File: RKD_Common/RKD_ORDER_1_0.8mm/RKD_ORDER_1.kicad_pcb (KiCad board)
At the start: 2 copper layers, 98.8 x 99.4 mm, 53 parts, among them SW2 KEY_SWITCH

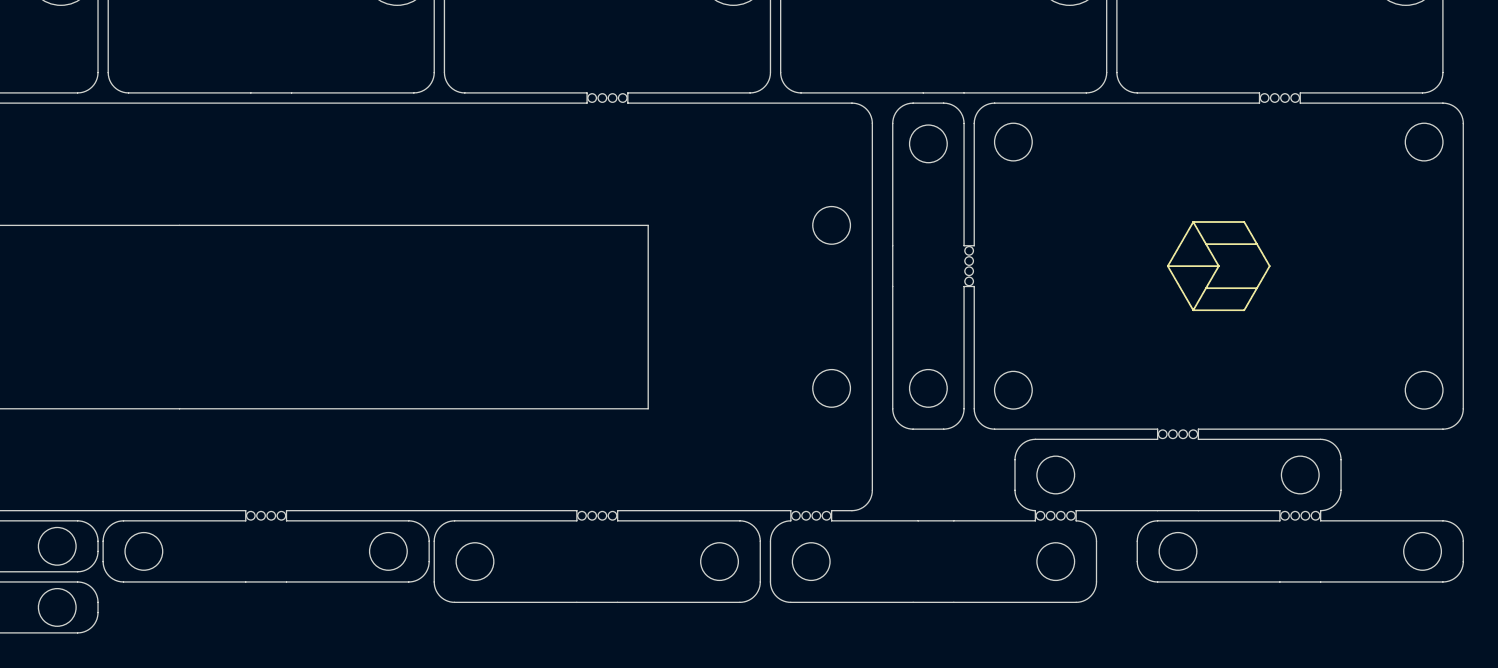
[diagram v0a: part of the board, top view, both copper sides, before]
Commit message: Order用の内容を削減
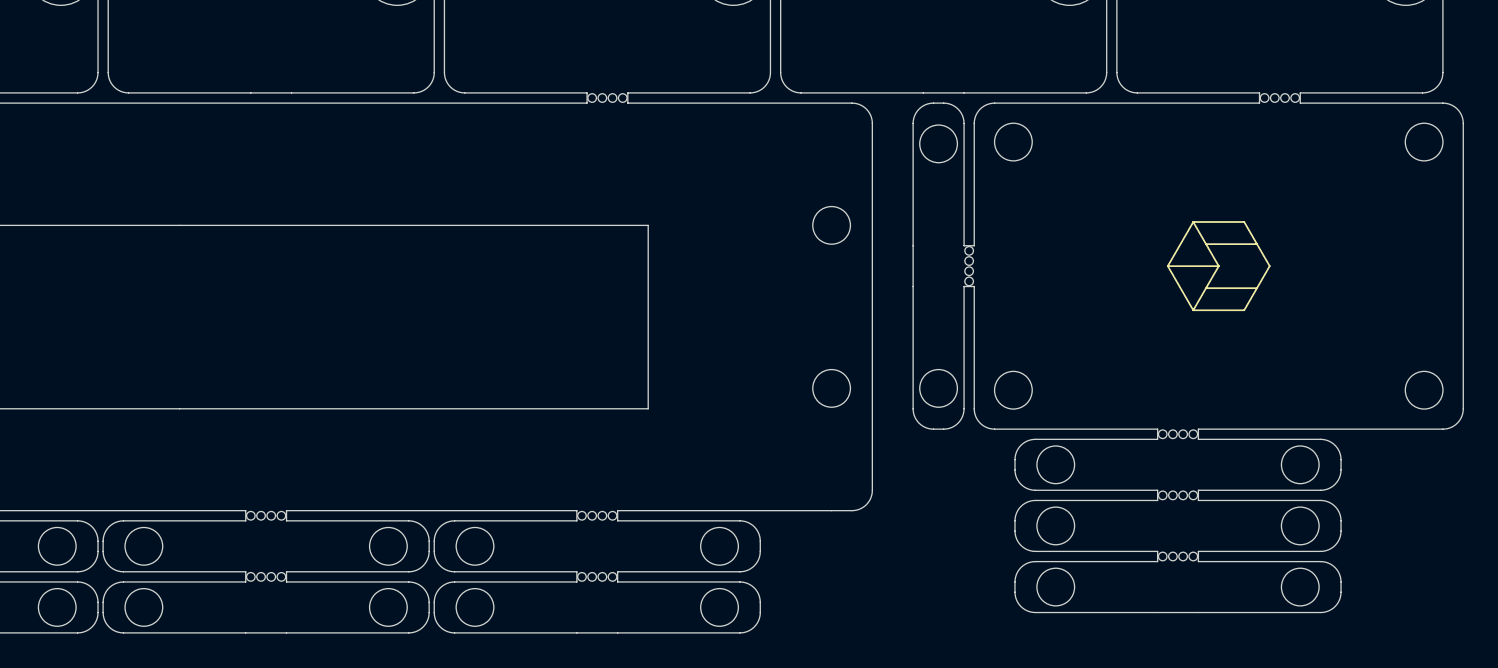
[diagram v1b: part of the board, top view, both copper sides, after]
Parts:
- removed the REF** at (91.7, 149.7)
- removed the REF** at (120.3, 149.7)
- removed the REF** at (106.0, 149.7)
- removed the Ref** at (91.7, 152.4)
- removed the Ref** at (98.5, 128.0)
- removed the Ref** at (106.0, 147.3)
- removed the Ref** at (127.4, 151.8)
- removed the Ref** at (72.0, 152.4)
- removed the Ref** at (120.3, 147.3)
- removed the Ref** at (52.7, 151.8)
- removed the Ref** at (113.1, 151.8)
- removed the Ref** at (98.5, 142.3)
- removed the Ref** at (67.0, 151.8)
- removed the Ref** at (86.3, 152.4)
- removed the Ref** at (106.0, 152.4)
- added REF**: rkd_cutdot, Rikkodo_FootPrint:rkd_cutdot, F.Cu at (113.1, 152.1)
- added REF**: rkd_cutdot, Rikkodo_FootPrint:rkd_cutdot, F.Cu at (113.1, 148.5)
- added REF**: rkd_cutdot, Rikkodo_FootPrint:rkd_cutdot, F.Cu at (59.8, 153.3)
- added REF**: rkd_cutdot, Rikkodo_FootPrint:rkd_cutdot, F.Cu at (79.2, 153.3)
- added Ref**: Val**, kbd_Hole:m2_Screw_Hole, F.Cu at (99.1, 142.3)
- added Ref**: Val**, kbd_Hole:m2_Screw_Hole, F.Cu at (106.0, 146.7)
- added Ref**: Val**, kbd_Hole:m2_Screw_Hole, F.Cu at (52.7, 151.5)
- added Ref**: Val**, kbd_Hole:m2_Screw_Hole, F.Cu at (72.0, 155.1)
- added Ref**: Val**, kbd_Hole:m2_Screw_Hole, F.Cu at (67.0, 151.5)
- added Ref**: Val**, kbd_Hole:m2_Screw_Hole, F.Cu at (52.7, 155.1)
- added Ref**: Val**, kbd_Hole:m2_Screw_Hole, F.Cu at (120.3, 153.9)
- added Ref**: Val**, kbd_Hole:m2_Screw_Hole, F.Cu at (120.3, 150.3)
- added Ref**: Val**, kbd_Hole:m2_Screw_Hole, F.Cu at (86.3, 151.5)
- added Ref**: Val**, kbd_Hole:m2_Screw_Hole, F.Cu at (86.3, 155.1)
- added Ref**: Val**, kbd_Hole:m2_Screw_Hole, F.Cu at (67.0, 155.1)
- added Ref**: Val**, kbd_Hole:m2_Screw_Hole, F.Cu at (99.1, 128.0)
- added Ref**: Val**, kbd_Hole:m2_Screw_Hole, F.Cu at (106.0, 150.3)
- added Ref**: Val**, kbd_Hole:m2_Screw_Hole, F.Cu at (72.0, 151.5)
- added Ref**: Val**, kbd_Hole:m2_Screw_Hole, F.Cu at (106.0, 153.9)
- added Ref**: Val**, kbd_Hole:m2_Screw_Hole, F.Cu at (120.3, 146.7)
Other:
- outline, holes or cut-outs redrawn
- board text removed: "RKD_PGD6 v1.0"
- board text removed: "RKD_PGD7 v1.0"
- board text removed: "RKD_PGD8 v1.0"

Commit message: SekiBall追加
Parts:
- added REF** (x2): rkd_SekiBall_ScrewHall, Rikkodo_FootPrint:rkd_SekiBall_ScrewHall, B.Cu at (115.5, 135.1)
- added REF** (x2): rkd_SekiBall_ScrewHall, Rikkodo_FootPrint:rkd_SekiBall_ScrewHall, B.Cu at (119.1, 72.0)

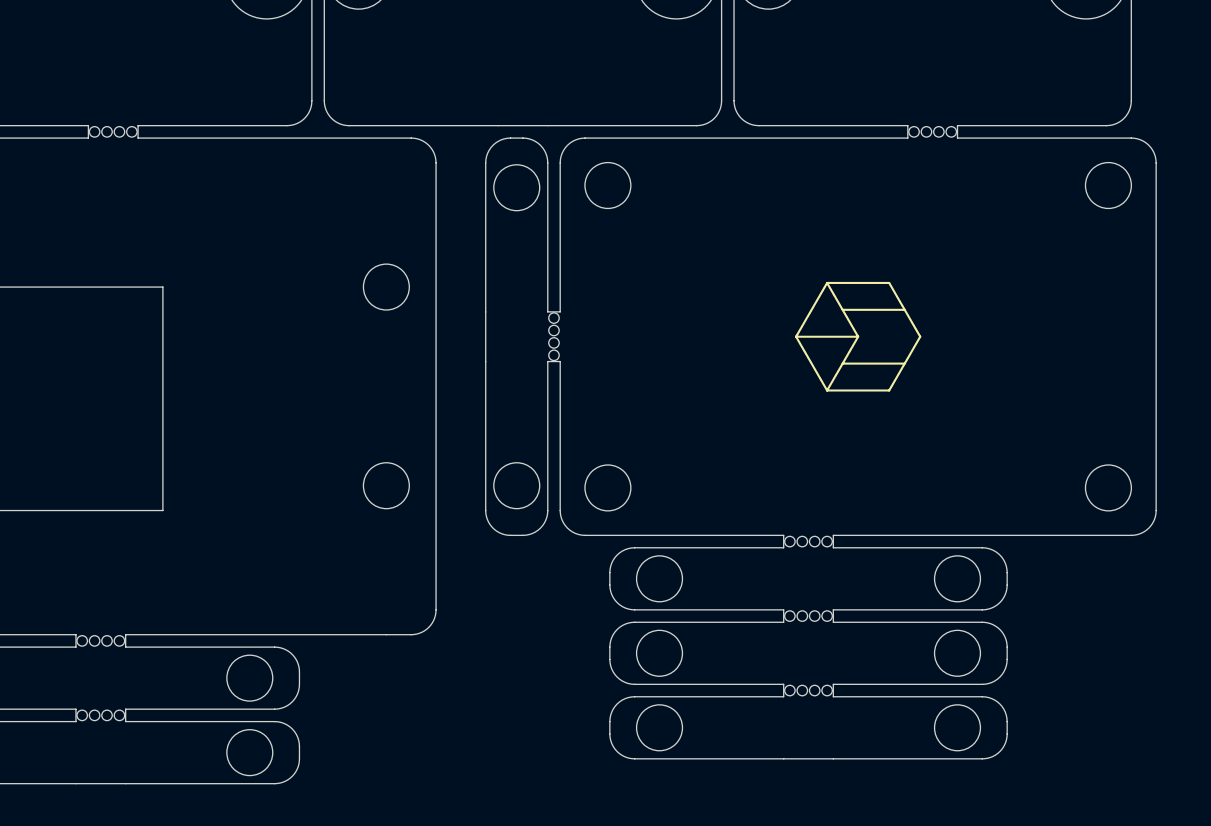
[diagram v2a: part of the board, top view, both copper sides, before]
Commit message: ワッシャー追加
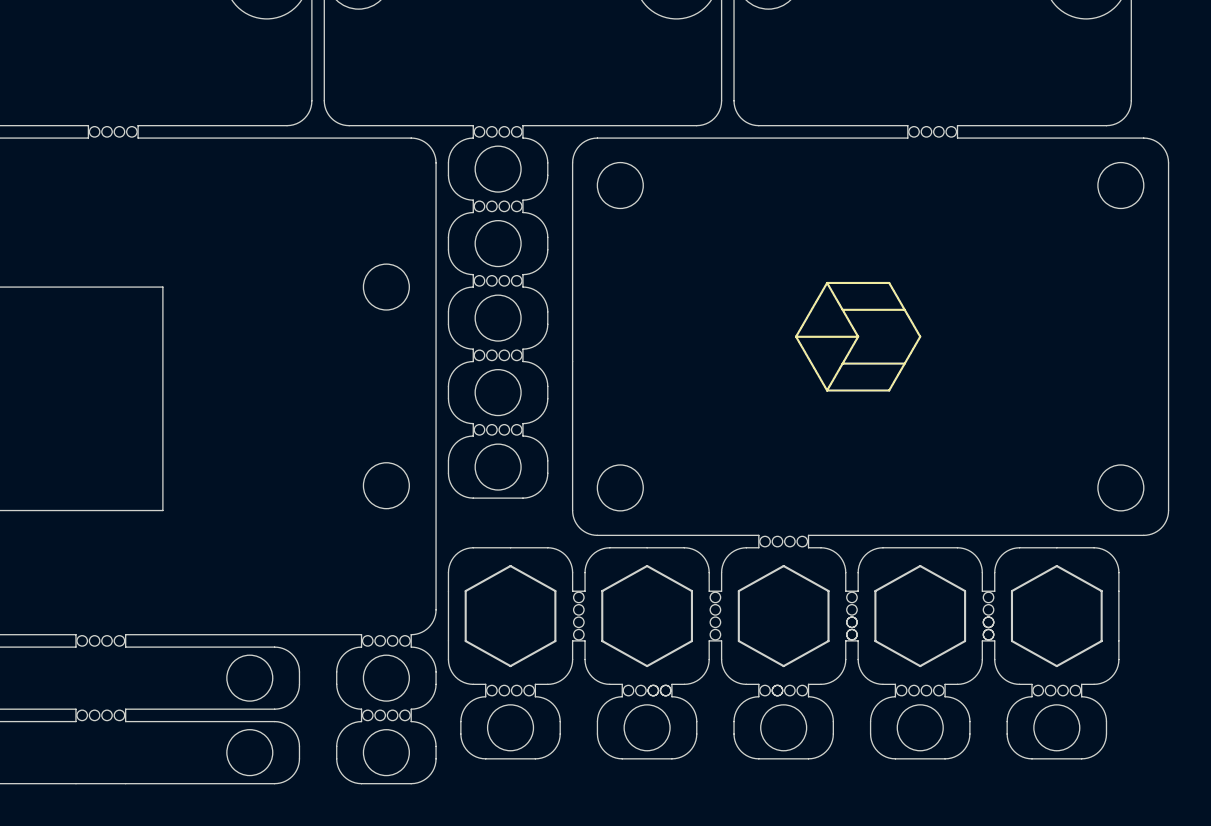
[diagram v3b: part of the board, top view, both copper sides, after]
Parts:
- removed the REF** at (113.1, 152.1)
- removed the REF** at (113.1, 148.5)
- removed the REF** at (100.9, 135.1)
- removed the REF** at (113.1, 145.0)
- removed the Ref** at (99.1, 142.3)
- removed the Ref** at (106.0, 146.7)
- removed the Ref** at (120.3, 153.9)
- removed the Ref** at (120.3, 150.3)
- removed the Ref** at (99.1, 128.0)
- removed the Ref** at (106.0, 150.3)
- removed the Ref** at (106.0, 153.9)
- removed the Ref** at (120.3, 146.7)
- added ?: , , F.Cu at (105.7, 152.1)
- added ?: , , F.Cu at (115.2, 149.4)
- added ?: , , F.Cu at (121.7, 149.4)
- added ?: , , F.Cu at (106.3, 152.1)
- added ?: , , F.Cu at (121.7, 148.8)
- added ?: , , F.Cu at (111.6, 152.1)
- added ?: , , F.Cu at (115.2, 148.8)
- added REF**: rkd_cutdot, Rikkodo_FootPrint:rkd_cutdot, F.Cu at (118.5, 152.1)
- added REF**: rkd_cutdot, Rikkodo_FootPrint:rkd_cutdot, F.Cu at (111.9, 145.0)
- added REF**: rkd_cutdot, Rikkodo_FootPrint:rkd_cutdot, F.Cu at (98.2, 128.9)
- added REF**: rkd_cutdot, Rikkodo_FootPrint:rkd_cutdot, F.Cu at (108.6, 148.5)
- added REF**: rkd_cutdot, Rikkodo_FootPrint:rkd_cutdot, F.Cu at (125.0, 152.1)
- added REF**: rkd_cutdot, Rikkodo_FootPrint:rkd_cutdot, F.Cu at (102.1, 148.5)
- added REF**: rkd_cutdot, Rikkodo_FootPrint:rkd_cutdot, F.Cu at (92.9, 153.3)
- added REF**: rkd_cutdot, Rikkodo_FootPrint:rkd_cutdot, F.Cu at (98.2, 136.0)
- added REF**: rkd_cutdot, Rikkodo_FootPrint:rkd_cutdot, F.Cu at (98.8, 152.1)
- added REF**: rkd_cutdot, Rikkodo_FootPrint:rkd_cutdot, F.Cu at (92.9, 149.7)
- added REF**: rkd_cutdot, Rikkodo_FootPrint:rkd_cutdot, F.Cu at (105.4, 152.1)
- added REF**: rkd_cutdot, Rikkodo_FootPrint:rkd_cutdot, F.Cu at (115.2, 148.5)
- added REF**: rkd_cutdot, Rikkodo_FootPrint:rkd_cutdot, F.Cu at (111.9, 152.1)
- added REF**: rkd_cutdot, Rikkodo_FootPrint:rkd_cutdot, F.Cu at (98.2, 125.3)
- added REF**: rkd_cutdot, Rikkodo_FootPrint:rkd_cutdot, F.Cu at (98.2, 132.5)
- added REF**: rkd_cutdot, Rikkodo_FootPrint:rkd_cutdot, F.Cu at (121.7, 148.5)
- added REF**: rkd_cutdot, Rikkodo_FootPrint:rkd_cutdot, F.Cu at (98.2, 139.6)
- added Ref**: Val**, kbd_Hole:m2_Screw_Hole, F.Cu at (98.2, 127.1)
- added Ref**: Val**, kbd_Hole:m2_Screw_Hole, F.Cu at (105.4, 153.9)
- added Ref**: Val**, kbd_Hole:m2_Screw_Hole, F.Cu at (98.2, 130.7)
- added Ref**: Val**, kbd_Hole:m2_Screw_Hole, F.Cu at (98.2, 134.2)
- added Ref**: Val**, kbd_Hole:m2_Spacer_Hole_hex, F.Cu at (105.4, 148.5)
- added Ref**: Val**, kbd_Hole:m2_Screw_Hole, F.Cu at (92.9, 151.5)
- added Ref**: Val**, kbd_Hole:m2_Screw_Hole, F.Cu at (125.0, 153.9)
- added Ref**: Val**, kbd_Hole:m2_Spacer_Hole_hex, F.Cu at (98.8, 148.5)
- added Ref**: Val**, kbd_Hole:m2_Spacer_Hole_hex, F.Cu at (118.5, 148.5)
- added Ref**: Val**, kbd_Hole:m2_Screw_Hole, F.Cu at (92.9, 155.1)
- added Ref**: Val**, kbd_Hole:m2_Screw_Hole, F.Cu at (118.5, 153.9)
- added Ref**: Val**, kbd_Hole:m2_Spacer_Hole_hex, F.Cu at (111.9, 148.5)
- added Ref**: Val**, kbd_Hole:m2_Spacer_Hole_hex, F.Cu at (125.0, 148.5)
- added Ref**: Val**, kbd_Hole:m2_Screw_Hole, F.Cu at (111.9, 153.9)
- added Ref**: Val**, kbd_Hole:m2_Screw_Hole, F.Cu at (98.8, 153.9)
- added Ref**: Val**, kbd_Hole:m2_Screw_Hole, F.Cu at (98.2, 141.4)
- added Ref**: Val**, kbd_Hole:m2_Screw_Hole, F.Cu at (98.2, 137.8)
- moved Point1 0.60 mm to (116.1, 135.1)
- moved REF** 0.60 mm to (116.1, 135.1) (x2)
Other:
- board size 98.8 x 99.4 mm -> 99.4 x 99.4 mm

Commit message: ORDER 不要パーツ削除
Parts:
- removed the ? at (105.7, 152.1)
- removed the ? at (115.2, 149.4)
- removed the ? at (121.7, 149.4)
- removed the ? at (106.3, 152.1)
- removed the ? at (121.7, 148.8)
- removed the ? at (111.6, 152.1)
- removed the ? at (115.2, 148.8)
- removed the REF** at (118.5, 152.1)
- removed the REF** at (111.9, 145.0)
- removed the REF** at (108.6, 148.5)
- removed the REF** at (125.0, 152.1)
- removed the REF** at (102.1, 148.5)
- removed the REF** at (98.8, 152.1)
- removed the REF** at (105.4, 152.1)
- removed the REF** at (115.2, 148.5)
- removed the REF** at (111.9, 152.1)
- removed the REF** at (121.7, 148.5)
- removed the Ref** at (105.4, 153.9)
- removed the Ref** at (105.4, 148.5)
- removed the Ref** at (125.0, 153.9)
- removed the Ref** at (98.8, 148.5)
- removed the Ref** at (118.5, 148.5)
- removed the Ref** at (118.5, 153.9)
- removed the Ref** at (111.9, 148.5)
- removed the Ref** at (125.0, 148.5)
- removed the Ref** at (111.9, 153.9)
- removed the Ref** at (98.8, 153.9)
- added ?: , , F.Cu at (127.7, 148.5)
- added ?: , , F.Cu at (107.5, 148.5)
- added ?: , , F.Cu at (122.6, 148.5)
- added ?: , , F.Cu at (117.6, 148.5)
- added ?: , , F.Cu at (112.5, 148.5)
- added REF**: rkd_cutdot, Rikkodo_FootPrint:rkd_cutdot, F.Cu at (117.9, 152.1)
- added REF**: rkd_cutdot, Rikkodo_FootPrint:rkd_cutdot, F.Cu at (107.8, 152.1)
- added REF**: rkd_cutdot, Rikkodo_FootPrint:rkd_cutdot, F.Cu at (117.9, 145.0)
- added REF**: rkd_cutdot, Rikkodo_FootPrint:rkd_cutdot, F.Cu at (122.9, 148.5)
- added REF**: rkd_cutdot, Rikkodo_FootPrint:rkd_cutdot, F.Cu at (107.8, 148.5)
- added REF**: rkd_cutdot, Rikkodo_FootPrint:rkd_cutdot, F.Cu at (122.9, 152.1)
- added REF**: rkd_cutdot, Rikkodo_FootPrint:rkd_cutdot, F.Cu at (107.8, 145.0)
- added REF**: rkd_cutdot, Rikkodo_FootPrint:rkd_cutdot, F.Cu at (112.8, 152.1)
- added REF**: rkd_cutdot, Rikkodo_FootPrint:rkd_cutdot, F.Cu at (128.0, 152.1)
- added REF**: rkd_cutdot, Rikkodo_FootPrint:rkd_cutdot, F.Cu at (112.8, 148.5)
- added REF**: rkd_cutdot, Rikkodo_FootPrint:rkd_cutdot, F.Cu at (122.9, 145.0)
- added REF**: rkd_cutdot, Rikkodo_FootPrint:rkd_cutdot, F.Cu at (128.0, 145.0)
- added REF**: rkd_cutdot, Rikkodo_FootPrint:rkd_cutdot, F.Cu at (117.9, 148.5)
- added REF**: rkd_cutdot, Rikkodo_FootPrint:rkd_cutdot, F.Cu at (98.2, 146.7)
- added REF**: rkd_LOGO, Rikkodo_FootPrint:rkd_LOGO, F.Cu at (88.1, 138.1)
- added REF**: rkd_cutdot, Rikkodo_FootPrint:rkd_cutdot, F.Cu at (128.0, 148.5)
- added REF**: rkd_cutdot, Rikkodo_FootPrint:rkd_cutdot, F.Cu at (98.2, 150.3)
- added REF**: rkd_cutdot, Rikkodo_FootPrint:rkd_cutdot, F.Cu at (112.8, 145.0)
- added REF**: rkd_cutdot, Rikkodo_FootPrint:rkd_cutdot, F.Cu at (98.2, 143.2)
- added Ref**: Val**, kbd_Hole:m2_Screw_Hole, F.Cu at (107.8, 146.7)
- added Ref**: Val**, kbd_Hole:m2_Screw_Hole, F.Cu at (128.0, 153.9)
- added Ref**: Val**, kbd_Hole:m2_Screw_Hole, F.Cu at (107.8, 153.9)
- added Ref**: Val**, kbd_Hole:m2_Screw_Hole, F.Cu at (112.8, 153.9)
- added Ref**: Val**, kbd_Hole:m2_Screw_Hole, F.Cu at (128.0, 150.3)
- added Ref**: Val**, kbd_Hole:m2_Screw_Hole, F.Cu at (122.9, 150.3)
- added Ref**: Val**, kbd_Hole:m2_Screw_Hole, F.Cu at (112.8, 150.3)
- added Ref**: Val**, kbd_Hole:m2_Screw_Hole, F.Cu at (98.2, 148.5)
- added Ref**: Val**, kbd_Hole:m2_Screw_Hole, F.Cu at (117.9, 146.7)
- added Ref**: Val**, kbd_Hole:m2_Screw_Hole, F.Cu at (122.9, 153.9)
- added Ref**: Val**, kbd_Hole:m2_Screw_Hole, F.Cu at (117.9, 150.3)
- added Ref**: Val**, kbd_Hole:m2_Screw_Hole, F.Cu at (98.2, 145.0)
- added Ref**: Val**, kbd_Hole:m2_Screw_Hole, F.Cu at (98.2, 152.1)
- added Ref**: Val**, kbd_Hole:m2_Screw_Hole, F.Cu at (122.9, 146.7)
- added Ref**: Val**, kbd_Hole:m2_Screw_Hole, F.Cu at (117.9, 153.9)
- added Ref**: Val**, kbd_Hole:m2_Screw_Hole, F.Cu at (107.8, 150.3)
- added Ref**: Val**, kbd_Hole:m2_Screw_Hole, F.Cu at (128.0, 146.7)
- added Ref**: Val**, kbd_Hole:m2_Screw_Hole, F.Cu at (112.8, 146.7)
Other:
- outline, holes or cut-outs redrawn
